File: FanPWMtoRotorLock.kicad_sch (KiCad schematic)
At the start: 23 parts, among them J1 0022232031, J2 0022232031, J3 0022232031, J4 0022232031, Q1 2N2907A, Q2 2N2222A, Q3 2N2907A, Q4 2N2222A, U1 NE556

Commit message: Inital board layout work
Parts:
- removed C2: 10uf, Capacitor_THT:CP_Radial_D5.0mm_P2.50mm, symbol Device:C_Polarized
- removed J3, J4: 0022232031, digikey-footprints:PinHeader_1x3_P2.54mm_Drill1.02mm, symbol dk_Rectangular-Connectors-Headers-Male-Pins:0022232031
- removed Q1, Q3: 2N2907A, Package_TO_SOT_THT:TO-92, symbol Simulation_SPICE:PNP
- removed Q2, Q4: 2N2222A, Package_TO_SOT_THT:TO-92, symbol Simulation_SPICE:NPN
- removed R10, R11, R12, R7, R8: 10K, Resistor_THT:R_Axial_DIN0309_L9.0mm_D3.2mm_P2.54mm_Vertical, symbol Device:R
- removed R9: 100, Resistor_THT:R_Axial_DIN0309_L9.0mm_D3.2mm_P2.54mm_Vertical, symbol Device:R
- removed U1: NE556, Package_DIP:DIP-14_W7.62mm, symbol Timer:NE556
- added Q2: MMBT2222A-7-F, digikey-footprints:SOT-23-3, symbol dk_Transistors-Bipolar-BJT-Single:MMBT2222A-7-F
- added Q3: MMBT2907ALT1G, digikey-footprints:SOT-23-3, symbol dk_Transistors-Bipolar-BJT-Single:MMBT2907ALT1G
- added U1: NE555P, Package_SO:SOIC-8_3.9x4.9mm_P1.27mm, symbol Timer:NE555P
- C1: footprint Capacitor_THT:CP_Radial_D5.0mm_P2.50mm -> Capacitor_SMD:C_0805_2012Metric_Pad1.18x1.45mm_HandSolder
- J1: Name In1 -> Fan1
- J2: footprint digikey-footprints:PinHeader_1x3_P2.54mm_Drill1.02mm -> Connector_JST:JST_PH_B3B-PH-K_1x03_P2.00mm_Vertical; Name Out1 -> Src1
- R1, R2, R3, R4, R5, R6: footprint Resistor_THT:R_Axial_DIN0309_L9.0mm_D3.2mm_P2.54mm_Vertical -> Resistor_SMD:R_0805_2012Metric_Pad1.20x1.40mm_HandSolder
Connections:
- net at C1.2, J1.1, J2.1: now also Q2.2 (E), Q3.2 (C), U1.1 (GND)
- net at R5.1: now also U1.3 (Q)
- net at R5.2: now also Q2.1 (B)
- net at J1.2, J2.2, R1.1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: now also U1.4 (R), U1.8 (VCC)
- net at J2.3, R6.2: now also Q2.3 (C)
- net at C1.1, R4.2: now also Q3.3 (E)
- net at R3.2, R4.1: now also U1.6 (THR), U1.7 (DIS)
- net at R2.2: now also Q3.1 (B), U1.2 (TR)
- no-connect marks 2 -> 1

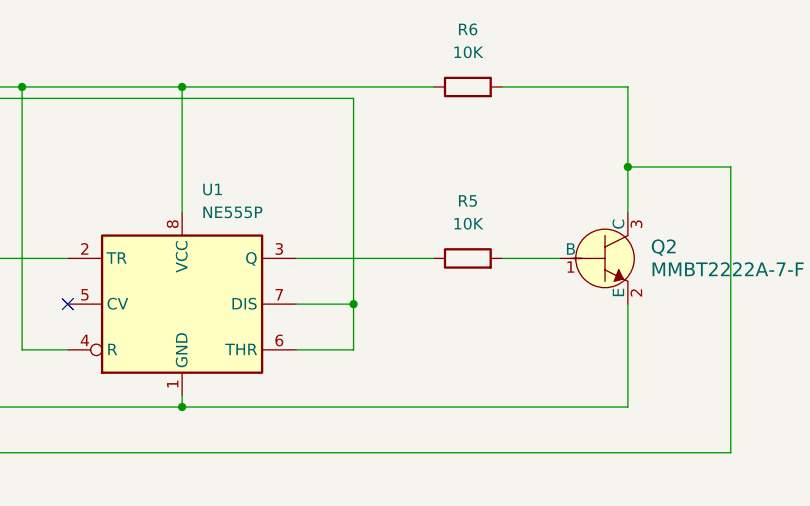
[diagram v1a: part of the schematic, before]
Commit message: Added decoupling cap, shrunk board layout
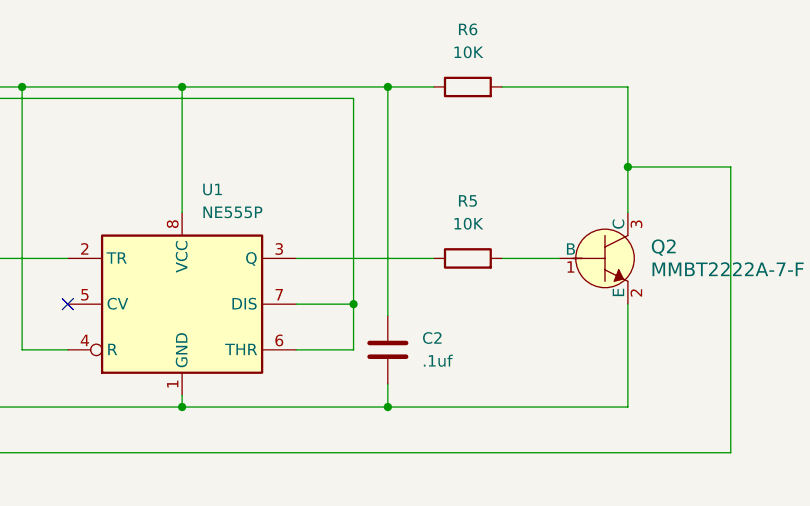
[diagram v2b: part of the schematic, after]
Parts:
- added C2: .1uf, Capacitor_SMD:C_0805_2012Metric_Pad1.18x1.45mm_HandSolder, symbol Device:C
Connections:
- net at C1.2, J1.1, J2.1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: now also C2.2
- net at J1.2, J2.2, R1.1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: now also C2.1
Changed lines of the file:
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@@
+	)
+	(junction
+		(at 205.74 82.55)
+		(diameter 0)
+		(color 0 0 0 0)
 	)
 	(junction
@@
 	(junction
 		(at 86.36 62.23)
+		(diameter 0)
+		(color 0 0 0 0)
+	)
+	(junction
+		(at 205.74 46.99)
 		(diameter 0)
 		(color 0 0 0 0)
@@
 	(wire
 		(pts
+			(xy 205.74 46.99) (xy 210.82 46.99)
+		)
+		(stroke
+			(width 0)
+			(type default)
+		)
+	)
+	(wire
+		(pts
 			(xy 218.44 66.04) (xy 224.79 66.04)
 		)
@@
 	(wire
 		(pts
+			(xy 205.74 80.01) (xy 205.74 82.55)
+		)
+		(stroke
+			(width 0)
+			(type default)
+		)
+	)
+	(wire
+		(pts
 			(xy 82.55 82.55) (xy 128.27 82.55)
 		)
@@
 	(wire
 		(pts
+			(xy 182.88 82.55) (xy 205.74 82.55)
+		)
+		(stroke
+			(width 0)
+			(type default)
+		)
+	)
+	(wire
+		(pts
 			(xy 243.84 55.88) (xy 243.84 87.63)
 		)
@@
 	(wire
 		(pts
-			(xy 182.88 46.99) (xy 210.82 46.99)
-		)
-		(stroke
-			(width 0)
-			(type default)
-		)
-	)
-	(wire
-		(pts
-			(xy 232.41 82.55) (xy 182.88 82.55)
+			(xy 182.88 46.99) (xy 205.74 46.99)
 		)
 		(stroke
@@
 	(wire
 		(pts
+			(xy 205.74 82.55) (xy 232.41 82.55)
+		)
+		(stroke
+			(width 0)
+			(type default)
+		)
+	)
+	(wire
+		(pts
 			(xy 86.36 46.99) (xy 86.36 57.15)
+		)
+		(stroke
+			(width 0)
+			(type default)
+		)
+	)
+	(wire
+		(pts
+			(xy 205.74 46.99) (xy 205.74 72.39)
 		)
 		(stroke
@@
 					(unit 1)
 				)
+			)
+		)
+	)
+	(symbol
+		(lib_id "Device:C")
+		(at 205.74 76.2 0)
+		(unit 1)
+		(exclude_from_sim no)
+		(in_bom yes)
+		(on_board yes)
+		(dnp no)
+		(fields_autoplaced yes)
+		(property "Reference" "C2"
+			(at 209.55 74.9299 0)
+			(effects
+				(font
+					(size 1.27 1.27)
+				)
+				(justify left)
+			)
+		)
+		(property "Value" ".1uf"
+			(at 209.55 77.4699 0)
+			(effects
+				(font
+					(size 1.27 1.27)
+				)
+				(justify left)
+			)
+		)
+		(property "Footprint" "Capacitor_SMD:C_0805_2012Metric_Pad1.18x1.45mm_HandSolder"
+			(at 206.7052 80.01 0)
+			(effects
+				(font
+					(size 1.27 1.27)
+				)
+				(hide yes)
+			)
+		)
+		(property "Datasheet" "~"
+			(at 205.74 76.2 0)
+			(effects
+				(font
+					(size 1.27 1.27)
+				)
+				(hide yes)
+			)
+		)
+		(property "Description" "Unpolarized capacitor"
+			(at 205.74 76.2 0)
+			(effects
+				(font
+					(size 1.27 1.27)
+				)
+				(hide yes)
+			)
+		)
+		(pin "2"
+		)
+		(pin "1"
+		)
+		(instances
+			(project ""
+				(path "/c0099403-d42d-41be-a2ae-764c0561f33a"
+					(reference "C2")
+					(unit 1)
+				)
